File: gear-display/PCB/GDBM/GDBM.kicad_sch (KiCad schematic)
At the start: 0 parts

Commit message: updates
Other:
- note added: "Analogi-inputin skaala? Patikannuppi Mitä ulostuloja"
- note removed: "LED sarjavastukset mitoitus Miksi MCU on 3v3? Analogi-inputin skaala? Patikannuppi"

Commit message: updates
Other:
- sheet Buttons renamed Brightness Control
- removed sheet Level Shifter
- note added: "MCU:n signaalien kytkeminen Voiko 3v3 dropata? Sim hub referenssipiiri?"
- note removed: "Analogi-inputin skaala? Patikannuppi Mitä ulostuloja"

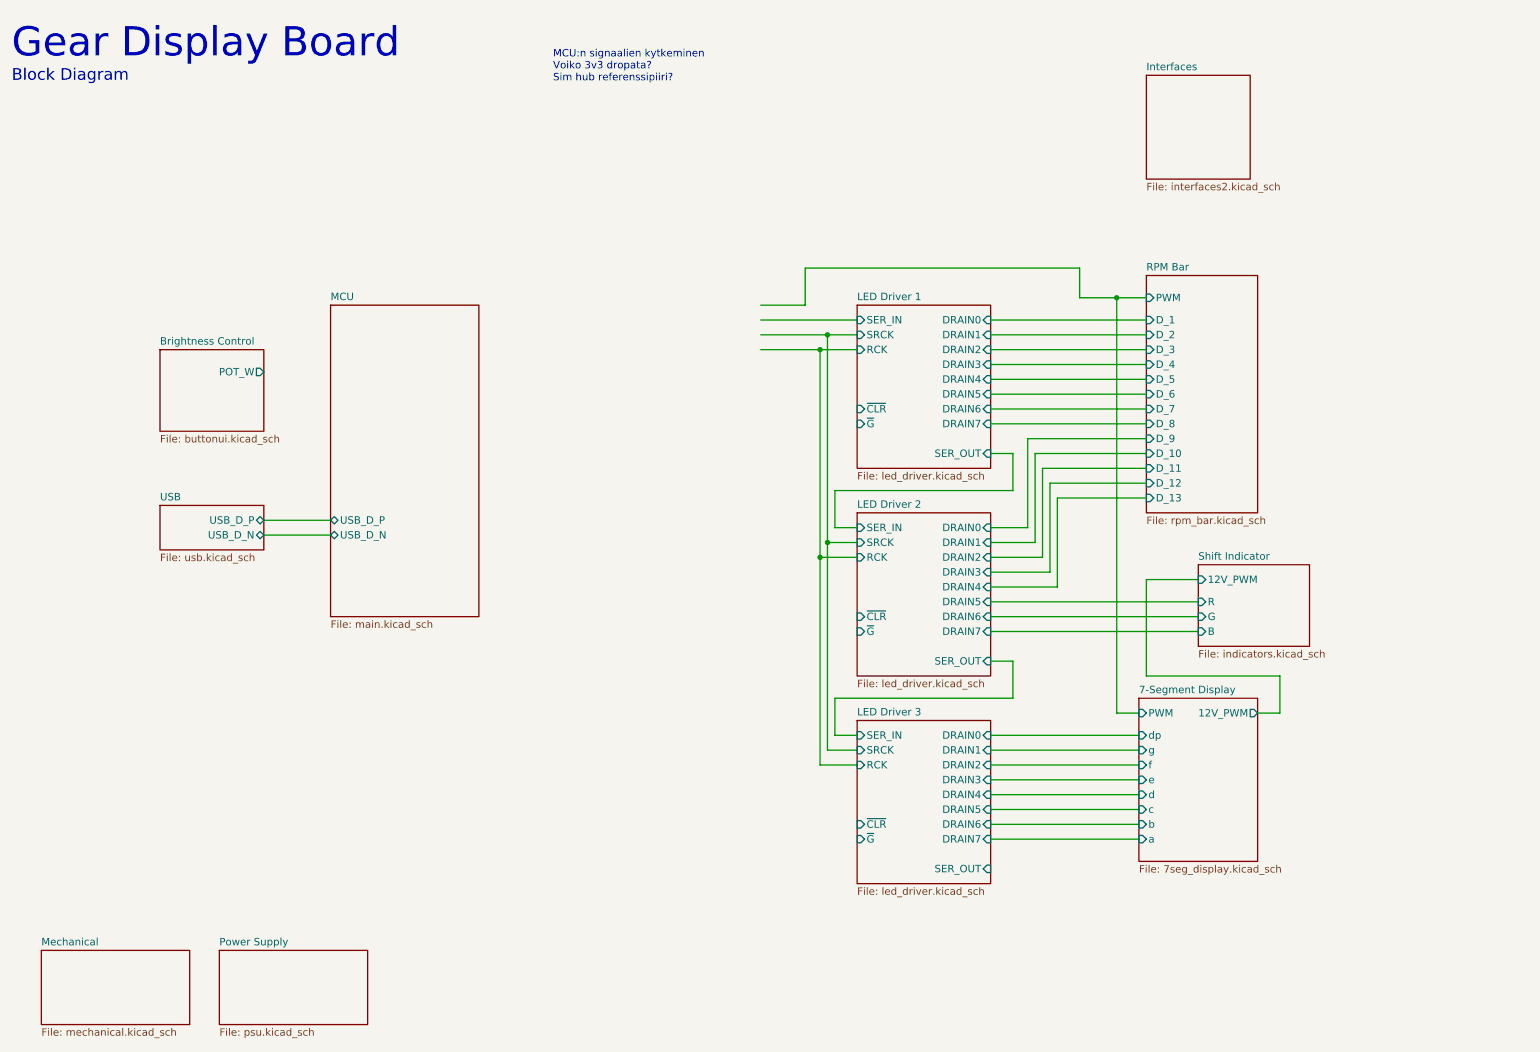
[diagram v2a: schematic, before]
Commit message: changed to match simhub conf
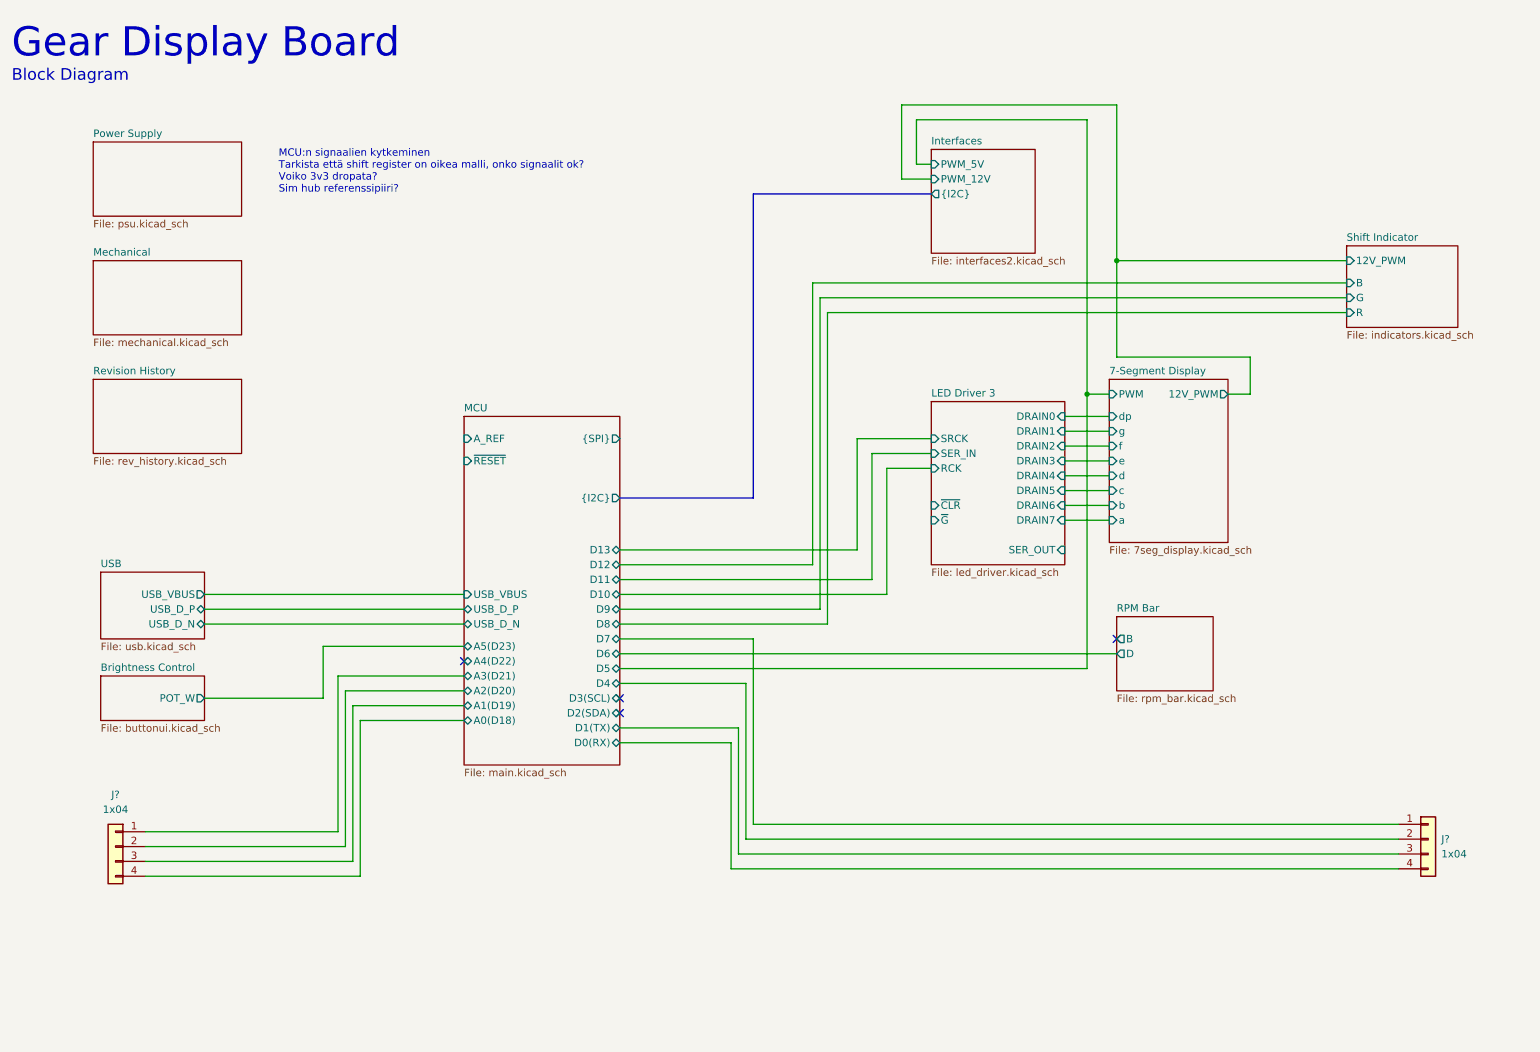
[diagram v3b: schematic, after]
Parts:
- added J? (x2): Con_Screw_1x04_691313510004, KD_Connector_Screw:CON_508_1X04_691313510004_Mated, symbol KD_Connector_Screw:Con_Screw_1x04_691313510004
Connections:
- new net MCU/A0(D18): J?.4 (Pin_4)
- new net MCU/A1(D19): J?.3 (Pin_3)
- new net MCU/A2(D20): J?.2 (Pin_2)
- new net MCU/A3(D21): J?.1 (Pin_1)
- new net MCU/D0(RX): J?.4 (Pin_4)
- new net MCU/D1(TX): J?.3 (Pin_3)
- new net MCU/D4: J?.2 (Pin_2)
- new net MCU/D7: J?.1 (Pin_1)
- no-connect marks 0 -> 4
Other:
- removed sheet LED Driver 1
- removed sheet LED Driver 2
- added sheet Revision History (rev_history.kicad_sch)
- sheet Interfaces ports: added PWM_12V, PWM_5V, {I2C}; removed none
- sheet MCU ports: added A0(D18), A1(D19), A2(D20), A3(D21), A4(D22), A5(D23), A_REF, D0(RX), D1(TX), D10, D11, D12, D13, D2(SDA), D3(SCL), D4, D5, D6, D7, D8, D9, USB_VBUS, {I2C}, {SPI}, ~{RESET}; removed none
- sheet RPM Bar ports: added B, D; removed D_1, D_10, D_11, D_12, D_13, D_2, D_3, D_4, D_5, D_6, D_7, D_8, D_9, PWM
- sheet USB ports: added USB_VBUS; removed none
- note added: "MCU:n signaalien kytkeminen Tarkista että shift register on oikea malli, onko signaalit ok? Voiko 3v3 dropata? Sim hub referenssipiiri?"
- note removed: "MCU:n signaalien kytkeminen Voiko 3v3 dropata? Sim hub referenssipiiri?"

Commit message: rikki
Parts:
- gave numbers to parts that had none: 2
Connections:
- no-connect marks 4 -> 10
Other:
- sheet RPM Bar ports: added LED_STRIP_B, LED_STRIP_D; removed B, D
- sheet Shift Indicator ports: added INDICATOR_B, INDICATOR_G, INDICATOR_R; removed B, G, R
- note added: "MCU:n signaalien kytkeminen Tarkista että shift register on oikea malli, onko signaalit ok?"
- note removed: "MCU:n signaalien kytkeminen Tarkista että shift register on oikea malli, onko signaalit ok? Voiko 3v3 dropata? Sim hub referenssipiiri?"

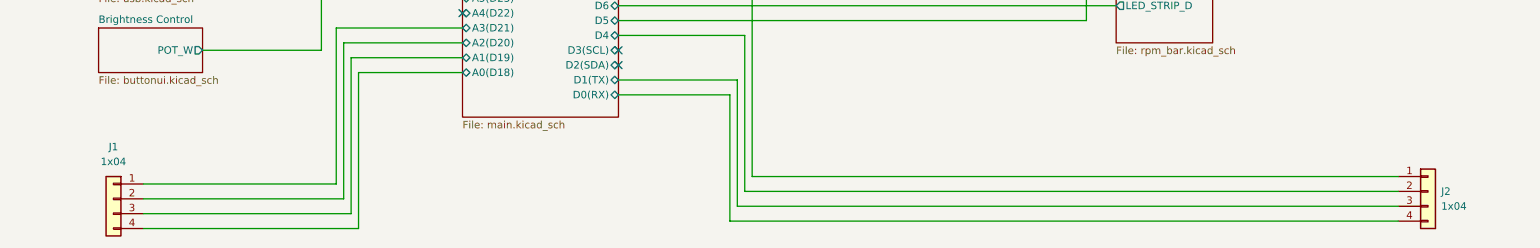
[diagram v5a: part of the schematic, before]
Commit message: PSU and LED powering changed
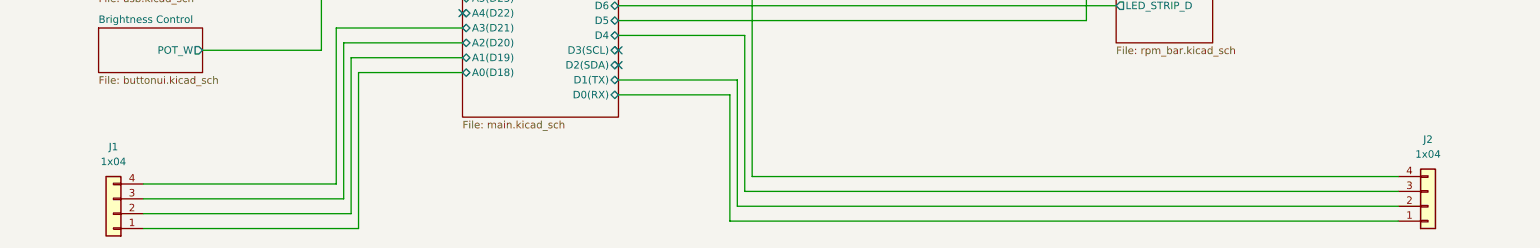
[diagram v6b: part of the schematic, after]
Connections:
- net MCU/A0(D18): now also J1.1 (Pin_1); no longer J1.4 (Pin_4)
- net MCU/A1(D19): now also J1.2 (Pin_2); no longer J1.3 (Pin_3)
- net MCU/A2(D20): now also J1.3 (Pin_3); no longer J1.2 (Pin_2)
- net MCU/A3(D21): now also J1.4 (Pin_4); no longer J1.1 (Pin_1)
- net MCU/D0(RX): now also J2.1 (Pin_1); no longer J2.4 (Pin_4)
- net MCU/D1(TX): now also J2.2 (Pin_2); no longer J2.3 (Pin_3)
- net MCU/D4: now also J2.3 (Pin_3); no longer J2.2 (Pin_2)
- net MCU/D7: now also J2.4 (Pin_4); no longer J2.1 (Pin_1)

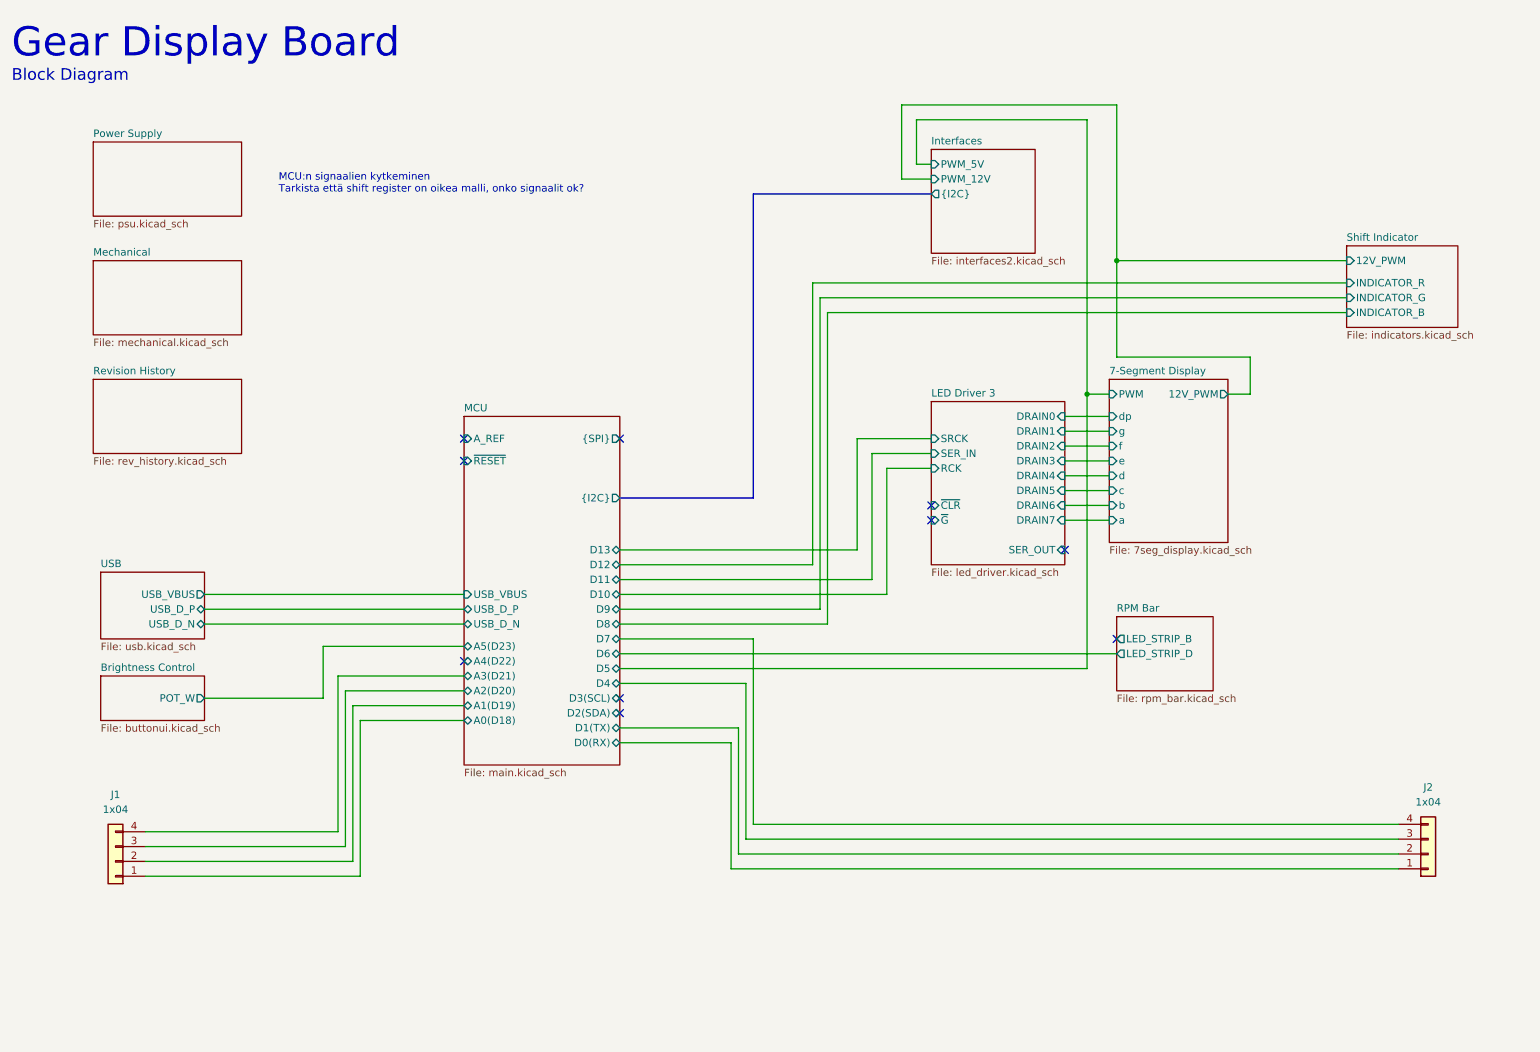
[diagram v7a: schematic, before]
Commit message: bugfixes
added 555 circuit for brightness control
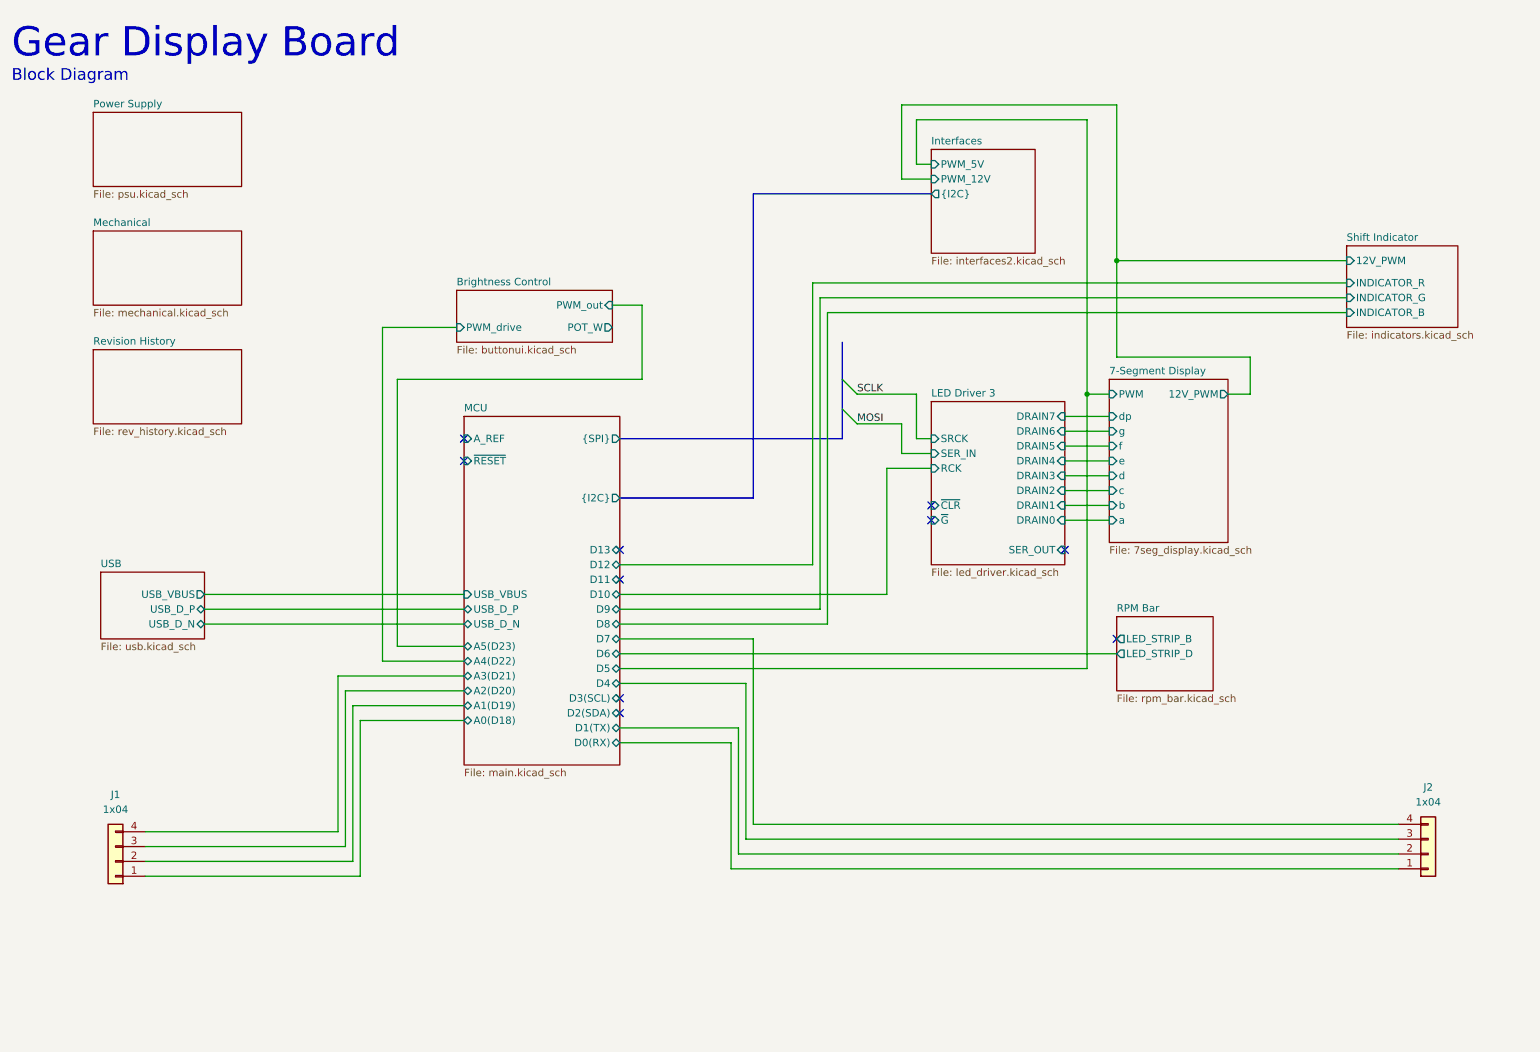
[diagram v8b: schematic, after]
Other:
- sheet Brightness Control ports: added PWM_drive, PWM_out; removed none
- note removed: "MCU:n signaalien kytkeminen Tarkista että shift register on oikea malli, onko signaalit ok?"
